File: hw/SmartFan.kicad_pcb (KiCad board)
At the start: 2 copper layers, 115 x 56 mm, 60 parts, among them J1 Barrel_Jack, J2 JTAG_SWD, J3 BTLE_LED_Conn, J4 ANT_LED_Conn, J5 RGB_LED_Conn, J6 PB_Conn, J7 FAN_CONN, Q1 MMBT2222A-7-F, Q2 MMBT2222A-7-F, Q3 MMBT2222A-TP, Q4 MMBT2222A-TP, Q5 MMBT2222A-TP, Q6 MMBT2222A-7-F, Q7 MMBT2222A-7-F, Q8 MMBT2222A-7-F, U1 L7805CV, U2 LTV-816S-TA1, U3 LTV-816S-TA1, U4 LTV-816S-TA1, U5 LD1117S33CTR

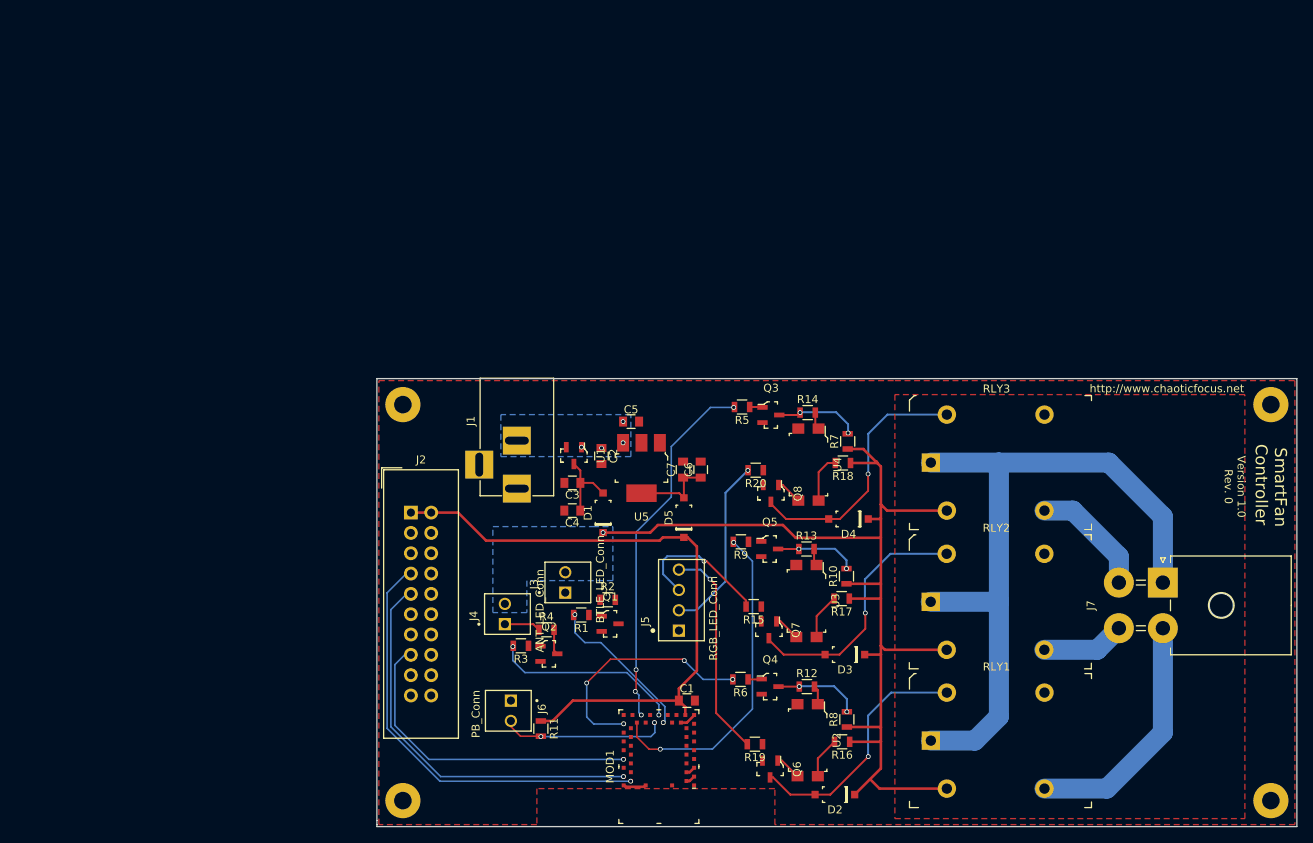
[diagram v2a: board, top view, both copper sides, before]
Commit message: Simplified schematic and pcb
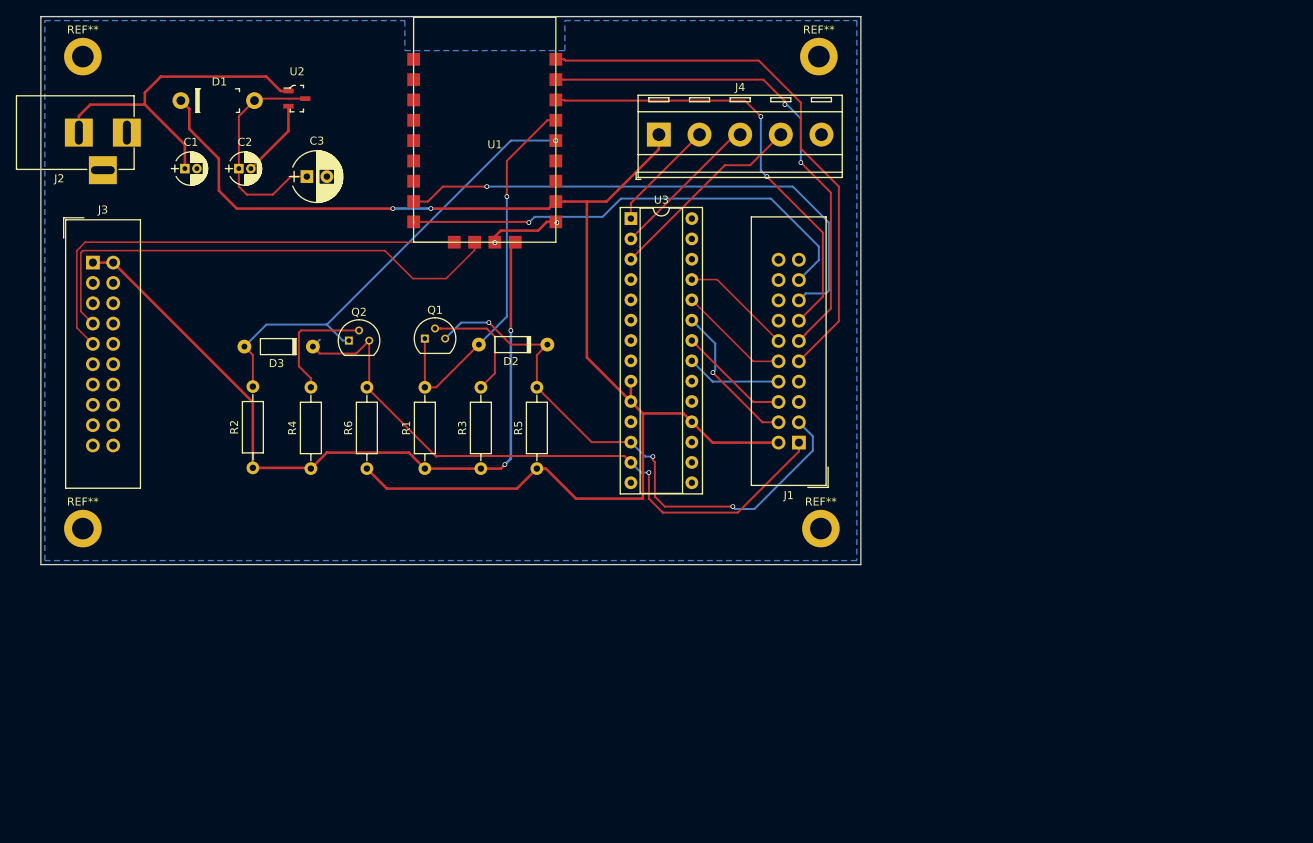
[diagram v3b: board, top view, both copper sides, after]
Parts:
- removed C4, C7: 0.1uF, Capacitors_SMD:C_0805
- removed C5, C6: 1uF, Capacitors_SMD:C_0805
- removed D4: 1N4148W-7-F, digikey-footprints:SOD-123
- removed D5: MBR0540T1G, digikey-footprints:SOD-123
- removed J5: RGB_LED_Conn, 640456-4:TE_640456-4
- removed J6: PB_Conn, 640456-2:TE_640456-2
- removed J7: FAN_CONN, Connectors_Molex:Molex_MegaFit_2x02x5.70mm_Angled
- removed MOD1: BMD-300-A-R, digikey-footprints:Bluetooth_Module_BMD-300
- removed Q3, Q4, Q5: MMBT2222A-TP, digikey-footprints:SOT-23-3
- removed Q6, Q7, Q8: MMBT2222A-7-F, digikey-footprints:SOT-23-3
- removed R10, R11, R7, R8: 10k, Resistors_SMD:R_0805
- removed R12, R13, R14, R16, R17, R18, R9: 1k, Resistors_SMD:R_0805
- removed R15, R19, R20: 330, Resistors_SMD:R_0805
- removed the REF** at (115.2, 83.2)
- removed the REF** at (115.2, 132.8)
- removed the REF** at (223.8, 132.8)
- removed the REF** at (223.8, 83.2)
- removed RLY1, RLY2, RLY3: G5LE-14_DC5, digikey-footprints:Relay_THT_G5LE-14
- removed U4: LTV-816S-TA1, digikey-footprints:SMD-4_4.6x7.62mm_P2.54mm
- removed U5: LD1117S33CTR, digikey-footprints:SOT-223
- added REF**: MountingHole_2.7mm_M2.5_DIN965_Pad, Mounting_Holes:MountingHole_2.7mm_M2.5_DIN965_Pad, F.Cu at (167.2, 39.8)
- added REF**: MountingHole_2.7mm_M2.5_DIN965_Pad, Mounting_Holes:MountingHole_2.7mm_M2.5_DIN965_Pad, F.Cu at (167.5, 98.8)
- added REF**: MountingHole_2.7mm_M2.5_DIN965_Pad, Mounting_Holes:MountingHole_2.7mm_M2.5_DIN965_Pad, F.Cu at (75.2, 39.8)
- added REF**: MountingHole_2.7mm_M2.5_DIN965_Pad, Mounting_Holes:MountingHole_2.7mm_M2.5_DIN965_Pad, F.Cu at (75.2, 98.8)
- C1: value 10uF -> 1uF; footprint Capacitors_SMD:C_0805 -> Capacitors_THT:CP_Radial_D4.0mm_P1.50mm
- C2: footprint Capacitors_SMD:C_0805 -> Capacitors_THT:CP_Radial_D4.0mm_P1.50mm
- C3: value 1uF -> 0.1uF; footprint Capacitors_SMD:C_0805 -> Capacitors_THT:CP_Radial_D6.3mm_P2.50mm
- D1: footprint digikey-footprints:SOD-123 -> digikey-footprints:DO-41
- D2, D3: value 1N4148W-7-F -> 1N914BTR; footprint digikey-footprints:SOD-123 -> digikey-footprints:DO-35
- J1: value Barrel_Jack -> DISPLAY; footprint Connectors:BARREL_JACK -> Connectors_IDC:IDC-Header_2x10_Pitch2.54mm_Straight
- J2: value JTAG_SWD -> Barrel_Jack; footprint Connectors_IDC:IDC-Header_2x10_Pitch2.54mm_Straight -> Connectors:BARREL_JACK
- J3: value BTLE_LED_Conn -> JTAG_SWD; footprint 640456-2:TE_640456-2 -> Connectors_IDC:IDC-Header_2x10_Pitch2.54mm_Straight
- J4: value ANT_LED_Conn -> Relay_Terminal; footprint 640456-2:TE_640456-2 -> TerminalBlock_RND:TerminalBlock_RND_205-00290_Pitch5.08mm
- Q1, Q2: value MMBT2222A-7-F -> 2N3904; footprint digikey-footprints:SOT-23-3 -> TO_SOT_Packages_THT:TO-92_Molded_Narrow
- R1: value 220 -> 4.7k; footprint Resistors_SMD:R_0805 -> Resistors_THT:R_Axial_DIN0207_L6.3mm_D2.5mm_P10.16mm_Horizontal
- R2: value 330 -> 4.7k; footprint Resistors_SMD:R_0805 -> Resistors_THT:R_Axial_DIN0207_L6.3mm_D2.5mm_P10.16mm_Horizontal
- R3: value 220 -> 10k; footprint Resistors_SMD:R_0805 -> Resistors_THT:R_Axial_DIN0207_L6.3mm_D2.5mm_P10.16mm_Horizontal
- R4: value 330 -> 10k; footprint Resistors_SMD:R_0805 -> Resistors_THT:R_Axial_DIN0207_L6.3mm_D2.5mm_P10.16mm_Horizontal
- R5, R6: value 1k -> 4.7k; footprint Resistors_SMD:R_0805 -> Resistors_THT:R_Axial_DIN0207_L6.3mm_D2.5mm_P10.16mm_Horizontal
- U1: value L7805CV -> hackaBLE_0.3; footprint digikey-footprints:SOT-23-3 -> hackaBLE_0:hackaBLE_0.3
- U2: value LTV-816S-TA1 -> L7805CV; footprint digikey-footprints:SMD-4_4.6x7.62mm_P2.54mm -> digikey-footprints:SOT-23-3
- U3: value LTV-816S-TA1 -> MCP23017_SP; footprint digikey-footprints:SMD-4_4.6x7.62mm_P2.54mm -> Housings_DIP:DIP-28_W7.62mm_Socket
- moved U2 102.5 mm to (102.0, 45.0), turned to 0 degrees
- moved C1 91.4 mm to (88.0, 53.8)
- moved D3 76.8 mm to (104.0, 76.0)
- moved D1 73.8 mm to (87.5, 45.2), turned to 0 degrees
- moved J3 72.0 mm to (76.5, 65.5), turned to 0 degrees
- moved D2 66.8 mm to (133.3, 75.8)
- moved J4 64.2 mm to (147.2, 49.5), turned to 0 degrees
- moved J2 59.3 mm to (80.8, 49.2)
- moved C2 57.8 mm to (94.8, 53.8), turned to 0 degrees
- moved R6 53.6 mm to (110.8, 91.2), turned to 90 degrees
- moved U3 52.6 mm to (143.8, 60.0), turned to 0 degrees
- moved C3 50.7 mm to (103.2, 54.8), turned to 0 degrees
- moved R2 47.3 mm to (96.5, 91.2), turned to 90 degrees
- moved Q2 46.5 mm to (108.5, 75.2)
- moved Q1 42.5 mm to (118.0, 75.0)
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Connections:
- C1 pad 1: +3V3 -> +9V
- C2 pad 1: +9V -> Net-(C2-Pad1)
- C3 pad 1: Net-(C3-Pad1) -> Net-(C2-Pad1)
- D1 pad A: Net-(C3-Pad1) -> Net-(C2-Pad1)
- D2 pad K: +5V -> /SCL_5v
- D3 pad K: +5V -> /SDA_5v
- J1 pad 1: GND -> /SDA_5v
- J1 pad 2: +9V -> +5V
- J1 pad 3: Net-(J1-Pad3) -> /SCL_5v
- J2 pad 1: +3V3 -> GND
- J2 pad 2: +3V3 -> +9V
- J3 pad 1: Net-(J3-Pad1) -> +3V3
- J3 pad 2: +5V -> +3V3
- J4 pad 1: Net-(J4-Pad1) -> +5V
- J4 pad 2: +5V -> /HI_SPD_EN
- Q1 pad 1: Net-(Q1-Pad1) -> Net-(D2-PadA)
- Q1 pad 2: GND -> Net-(Q1-Pad2)
- Q1 pad 3: Net-(Q1-Pad3) -> /SCL_5v
- Q2 pad 1: Net-(Q2-Pad1) -> Net-(D3-PadA)
- Q2 pad 2: GND -> Net-(Q2-Pad2)
- Q2 pad 3: Net-(Q2-Pad3) -> /SDA_5v
- R1 pad 1: Net-(Q1-Pad1) -> +3V3
- R1 pad 2: /BTLE_LED -> Net-(D2-PadA)
- R2 pad 1: Net-(J3-Pad1) -> +3V3
- R2 pad 2: Net-(Q1-Pad3) -> Net-(D3-PadA)
- R3 pad 1: Net-(Q2-Pad1) -> +3V3
- R3 pad 2: /ANT_LED -> Net-(Q1-Pad2)
- R4 pad 1: Net-(J4-Pad1) -> +3V3
- R4 pad 2: Net-(Q2-Pad3) -> Net-(Q2-Pad2)
- R5 pad 1: Net-(Q3-Pad1) -> +5V
- R5 pad 2: Net-(MOD1-Pad27) -> /SCL_5v
- R6 pad 1: Net-(Q4-Pad1) -> +5V
- R6 pad 2: Net-(MOD1-Pad31) -> /SDA_5v
- U1 pad 1: +9V -> Net-(U1-Pad1)
- U1 pad 2: GND -> Net-(U1-Pad2)
- U1 pad 3: Net-(C3-Pad1) -> Net-(U1-Pad3)
- U2 pad 1: Net-(R12-Pad2) -> +9V
- U2 pad 3: Net-(Q6-Pad1) -> Net-(C2-Pad1)
- U3 pad 1: Net-(R13-Pad2) -> /HI_SPD_EN
- U3 pad 2: GND -> /MED_SPD_EN
- U3 pad 3: Net-(Q7-Pad1) -> /LO_SPD_EN
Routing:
- net /120VAC_IN: track 91.1 -> 0.00 mm
- net /SDA_5v: track 0.00 -> 82.0 mm, vias 0 -> 2
- net /SCL_5v: track 0.00 -> 71.5 mm, vias 0 -> 4
- net /ROT_ENC_A: track 0.00 -> 69.2 mm
- net /ROT_ENC_SW1: track 0.00 -> 67.3 mm, vias 0 -> 4
- net /ROT_ENC_B: track 0.00 -> 63.9 mm, vias 0 -> 2
- net /ROT_ENC_SW2: track 0.00 -> 59.6 mm, vias 0 -> 2
- net /ROT_ENC_C: track 0.00 -> 56.5 mm, vias 0 -> 2
- net Net-(MOD1-Pad27): track 45.7 -> 0.00 mm, vias 4 -> 0
- net +9V: track 0.38 -> 42.0 mm, vias 4 -> 0
- net Net-(MOD1-Pad28): track 40.9 -> 0.00 mm, vias 2 -> 0
- net /~RESET: track 40.5 -> 0.00 mm, vias 1 -> 0
- net +5V: track 134.8 -> 173.2 mm, vias 1 -> 2
- net Net-(D4-PadA): track 32.6 -> 0.00 mm, vias 1 -> 0
- net /LO_SPD_120VAC: track 30.7 -> 0.00 mm
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- added copper zone on B.Cu, net GND
- removed copper zone on B.Cu, net +5V
- removed copper zone on B.Cu, net +9V
- removed copper zone on F.Cu, net GND
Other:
- board size 115 x 56 mm -> 102.5 x 68.5 mm
- board text removed: "SmartFan Controller"
- board text removed: "Version 1.0 Rev. 0"
- board text removed: "http://www.chaoticfocus.net"

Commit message: Final v1 updates
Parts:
- removed the REF** at (167.2, 39.8)
- removed the REF** at (167.5, 98.8)
- removed the REF** at (75.2, 39.8)
- removed the REF** at (75.2, 98.8)
- added J5: Relay_Terminal, TerminalBlock_RND:TerminalBlock_RND_205-00290_Pitch5.08mm, F.Cu at (130.2, 104.3)
- added REF**: MountingHole_2.7mm_M2.5_Pad_Via, Mounting_Holes:MountingHole_2.7mm_M2.5_Pad_Via, F.Cu at (108.6, 64.6)
- added REF**: MountingHole_2.7mm_M2.5_Pad_Via, Mounting_Holes:MountingHole_2.7mm_M2.5_Pad_Via, F.Cu at (186.3, 64.7)
- added REF**: MountingHole_2.7mm_M2.5_Pad_Via, Mounting_Holes:MountingHole_2.7mm_M2.5_Pad_Via, F.Cu at (186.3, 112.6)
- added REF**: MountingHole_2.7mm_M2.5_Pad_Via, Mounting_Holes:MountingHole_2.7mm_M2.5_Pad_Via, F.Cu at (108.7, 112.6)
- D1: footprint digikey-footprints:DO-41 -> Digikey:DO-41
- D2, D3: footprint digikey-footprints:DO-35 -> Digikey:DO-35
- J3: value JTAG_SWD -> PWR_SW; footprint Connectors_IDC:IDC-Header_2x10_Pitch2.54mm_Straight -> Connectors:PINHEAD1-2
- J4: value Relay_Terminal -> JTAG_SWD; footprint TerminalBlock_RND:TerminalBlock_RND_205-00290_Pitch5.08mm -> Connectors_IDC:IDC-Header_2x10_Pitch2.54mm_Straight
- U2: footprint digikey-footprints:SOT-23-3 -> Digikey:SOT-23-3
- moved D3 75.8 mm to (173.2, 106.8), turned to 90 degrees
- moved J4 65.8 mm to (185.0, 103.3), turned to 180 degrees
- moved R2 62.0 mm to (157.2, 103.3), turned to 0 degrees
- moved D1 60.4 mm to (124.3, 93.1), turned to 180 degrees
- moved R4 56.2 mm to (157.2, 108.3), turned to 0 degrees
- moved Q2 55.1 mm to (159.0, 97.3)
- moved R6 51.5 mm to (157.2, 113.3), turned to 0 degrees
- moved J3 45.9 mm to (122.4, 66.6), turned to 180 degrees
- moved C1 45.3 mm to (111.8, 92.3), turned to 180 degrees
- moved U2 42.9 mm to (116.4, 85.4), turned to 180 degrees
- moved J2 42.2 mm to (115.2, 73.6)
- moved U1 37.4 mm to (153.2, 76.6)
- moved R1 37.3 mm to (153.2, 103.3), turned to 180 degrees
- moved C3 35.8 mm to (121.0, 85.8)
- moved C2 35.6 mm to (110.5, 85.6)
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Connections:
- C1 pad 1: +9V -> Net-(C1-Pad1)
- D2 pad A: Net-(D2-PadA) -> /SCL_3v3
- D3 pad A: Net-(D3-PadA) -> /SDA_3v3
- J1 pad 1: /SDA_5v -> /SDA_3v3
- J1 pad 3: /SCL_5v -> /SCL_3v3
- J3 pad 1: +3V3 -> Net-(C1-Pad1)
- J3 pad 2: +3V3 -> +9V
- J4 pad 1: +5V -> +3V3
- J4 pad 2: /HI_SPD_EN -> +3V3
- J4 pad 3: /MED_SPD_EN -> Net-(J4-Pad3)
- J4 pad 4: /LO_SPD_EN -> GND
- J4 pad 5: GND -> Net-(J4-Pad5)
- Q1 pad 1: Net-(D2-PadA) -> /SCL_3v3
- Q2 pad 1: Net-(D3-PadA) -> /SDA_3v3
- R1 pad 2: Net-(D2-PadA) -> /SCL_3v3
- R2 pad 2: Net-(D3-PadA) -> /SDA_3v3
- U1 pad 13: Net-(D2-PadA) -> /SCL_3v3
- U1 pad 14: Net-(D3-PadA) -> /SDA_3v3
- U2 pad 1: +9V -> Net-(C1-Pad1)
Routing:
- net /SCL_3v3: track 0.00 -> 109.7 mm, vias 0 -> 5
- net +5V: track 173.2 -> 111.2 mm
- net /SDA_3v3: track 0.00 -> 59.9 mm, vias 0 -> 2
- net Net-(D3-PadA): track 58.6 -> 0.00 mm, vias 1 -> 0
- net /ROT_ENC_A: track 69.2 -> 18.0 mm
- net Net-(D2-PadA): track 47.7 -> 0.00 mm, vias 1 -> 0
- net GND: track 18.9 -> 62.8 mm
- net /ROT_ENC_B: track 63.9 -> 22.5 mm, vias 2 -> 0
- net +3V3: track 97.2 -> 63.4 mm, vias 2 -> 0
- net /ROT_ENC_SW1: track 67.3 -> 34.3 mm, vias 4 -> 1
- net Net-(C1-Pad1): track 0.00 -> 31.5 mm, vias 0 -> 2
- net /HI_SPD_EN: track 14.1 -> 44.9 mm
- net /SCL_5v: track 71.5 -> 40.7 mm, vias 4 -> 0
- net +9V: track 42.0 -> 13.5 mm
- net /ROT_ENC_C: track 56.5 -> 28.0 mm, vias 2 -> 0
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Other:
- board size 102.5 x 68.5 mm -> 87.1 x 56.8 mm
- net class 120VAC removed
- net class Data removed
- net class Default: via_dia 0.6 -> 0.8
- net class PWR removed
- rule pad_to_mask_clearance: 0.2 -> 0
- board text added: "+"
- board text added: "-"
- board text added: "5v"
- board text added: "Display"
- board text added: "GND"
- board text added: "HI"
- board text added: "LO"
- board text added: "MED"
- board text added: "PWR SW"
- board text added: "Programming"
- board text added: "Smart Fan Controller v1.0"

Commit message: Hardware design updates
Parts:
- removed the REF** at (108.6, 64.6)
- removed the REF** at (186.3, 64.7)
- removed the REF** at (186.3, 112.6)
- removed the REF** at (108.7, 112.6)
- added REF**: MountingHole_3.2mm_M3_Pad, MountingHole:MountingHole_3.2mm_M3_Pad, F.Cu at (113.3, 118.4)
- added REF**: MountingHole_3.2mm_M3_Pad, MountingHole:MountingHole_3.2mm_M3_Pad, F.Cu at (113.3, 73.2)
- added REF**: MountingHole_3.2mm_M3_Pad, MountingHole:MountingHole_3.2mm_M3_Pad, F.Cu at (198.6, 118.4)
- added REF**: MountingHole_3.2mm_M3_Pad, MountingHole:MountingHole_3.2mm_M3_Pad, F.Cu at (198.6, 73.2)
- C1, C2: footprint Capacitors_THT:CP_Radial_D4.0mm_P1.50mm -> Capacitor_THT:CP_Radial_D4.0mm_P1.50mm
- C3: footprint Capacitors_THT:CP_Radial_D6.3mm_P2.50mm -> Capacitor_THT:CP_Radial_D6.3mm_P2.50mm
- D1: footprint Digikey:DO-41 -> digikey-footprints:DO-41
- D2, D3: footprint Digikey:DO-35 -> digikey-footprints:DO-35
- J1, J4: footprint Connectors_IDC:IDC-Header_2x10_Pitch2.54mm_Straight -> Connector_IDC:IDC-Header_2x10_P2.54mm_Vertical
- J2: value Barrel_Jack -> PJ-102A; footprint Connectors:BARREL_JACK -> digikey-footprints:Barrel_Jack_5.5mmODx2.1mmID_PJ-102A
- J3: footprint Connectors:PINHEAD1-2 -> Connector_PinHeader_2.54mm:PinHeader_1x02_P2.54mm_Vertical
- J5: footprint TerminalBlock_RND:TerminalBlock_RND_205-00290_Pitch5.08mm -> TerminalBlock_RND:TerminalBlock_RND_205-00290_1x05_P5.08mm_Horizontal
- Q1, Q2: footprint TO_SOT_Packages_THT:TO-92_Molded_Narrow -> digikey-footprints:TO-92-3
- R1, R2, R3, R4, R5, R6: footprint Resistors_THT:R_Axial_DIN0207_L6.3mm_D2.5mm_P10.16mm_Horizontal -> Resistor_THT:R_Axial_DIN0207_L6.3mm_D2.5mm_P10.16mm_Horizontal
- U2: footprint Digikey:SOT-23-3 -> digikey-footprints:SOT-23-3
- U3: footprint Housings_DIP:DIP-28_W7.62mm_Socket -> digikey-footprints:Socket_DIP-28_7.62mm_Conn
- moved D3 62.8 mm to (111.3, 97.0), turned to 0 degrees
- moved R2 47.2 mm to (110.7, 111.3)
- moved R4 46.5 mm to (110.7, 107.2)
- moved R6 38.0 mm to (120.9, 102.1), turned to 180 degrees
- moved Q2 31.4 mm to (129.5, 108.2), turned to 90 degrees
- moved U3 29.9 mm to (147.6, 86.9)
- moved J1 29.2 mm to (163.6, 117.9), turned to 90 degrees
- moved J5 26.4 mm to (134.0, 78.2), turned to 0 degrees
- moved Q1 25.5 mm to (129.5, 118.4), turned to 90 degrees
- moved R1 25.0 mm to (134.1, 119.4), turned to 0 degrees
- moved U1 24.5 mm to (176.3, 84.8)
- moved R3 20.4 mm to (134.1, 115.3), turned to 0 degrees
- moved C3 19.3 mm to (140.2, 87.9), turned to 270 degrees
- moved R5 19.3 mm to (134.1, 111.3), turned to 0 degrees
- moved J3 16.3 mm to (114.3, 80.8), turned to 0 degrees
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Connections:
- U3 pad 10: +5V -> GND
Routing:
- net /SDA_3v3: track 59.9 -> 133.4 mm, vias 2 -> 4
- net /ROT_ENC_A: track 18.0 -> 76.2 mm
- net GND: track 62.8 -> 12.2 mm, vias 2 -> 3
- net /ROT_ENC_B: track 22.5 -> 71.1 mm
- net +3V3: track 63.4 -> 106.9 mm, vias 0 -> 3
- net /ROT_ENC_C: track 28.0 -> 66.0 mm
- net /HI_SPD_EN: track 44.9 -> 12.2 mm
- net /MED_SPD_EN: track 42.9 -> 13.6 mm
- net /LO_SPD_EN: track 42.5 -> 14.5 mm, vias 1 -> 0
- net +5V: track 111.2 -> 131.8 mm, vias 2 -> 3
- net /SWDIO: track 46.3 -> 30.3 mm
- net /RGB_Y: track 33.8 -> 19.4 mm, vias 1 -> 2
- net /RGB_G: track 35.9 -> 24.5 mm, vias 0 -> 2
- net /SDA_5v: track 61.4 -> 50.4 mm
- net /ROT_ENC_SW2: track 41.1 -> 30.2 mm, vias 1 -> 2
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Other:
- board size 87.1 x 56.8 mm -> 93.5 x 53.3 mm
- net class 3v added: clearance 0.2, trace_width 0.3, via_dia 0.8, via_drill 0.4
- net class 5v added: clearance 0.2, trace_width 0.35, via_dia 0.8, via_drill 0.4
- net class 9v added: clearance 0.2, trace_width 0.35, via_dia 0.8, via_drill 0.4
- net class GND added: clearance 0.2, trace_width 0.3, via_dia 0.8, via_drill 0.4
- board text added: "Power Sw"
- board text added: "Relays"
- board text added: "Smart Fan Controller v1.1 Rev. 0"
- board text removed: "+"
- board text removed: "-"
- board text removed: "5v"
- board text removed: "GND"
- board text removed: "HI"
- board text removed: "LO"
- board text removed: "MED"
- board text removed: "PWR SW"
- board text removed: "Smart Fan Controller v1.0"
